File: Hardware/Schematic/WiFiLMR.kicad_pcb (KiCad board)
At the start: 2 copper layers, 50 parts, among them J1 Conn_01x12, J10 Conn_01x02, J2 Conn_01x12, J3 JTAG, J4 Conn_02x04_Odd_Even, J5 Conn_02x02_Odd_Even, J6 Conn_01x12, J7 Conn_01x12, J8 Conn_01x24, J9 Conn_01x02, Q1 Q_PJFET_GSD, U1 TCA8418RTWR, U2 L7805

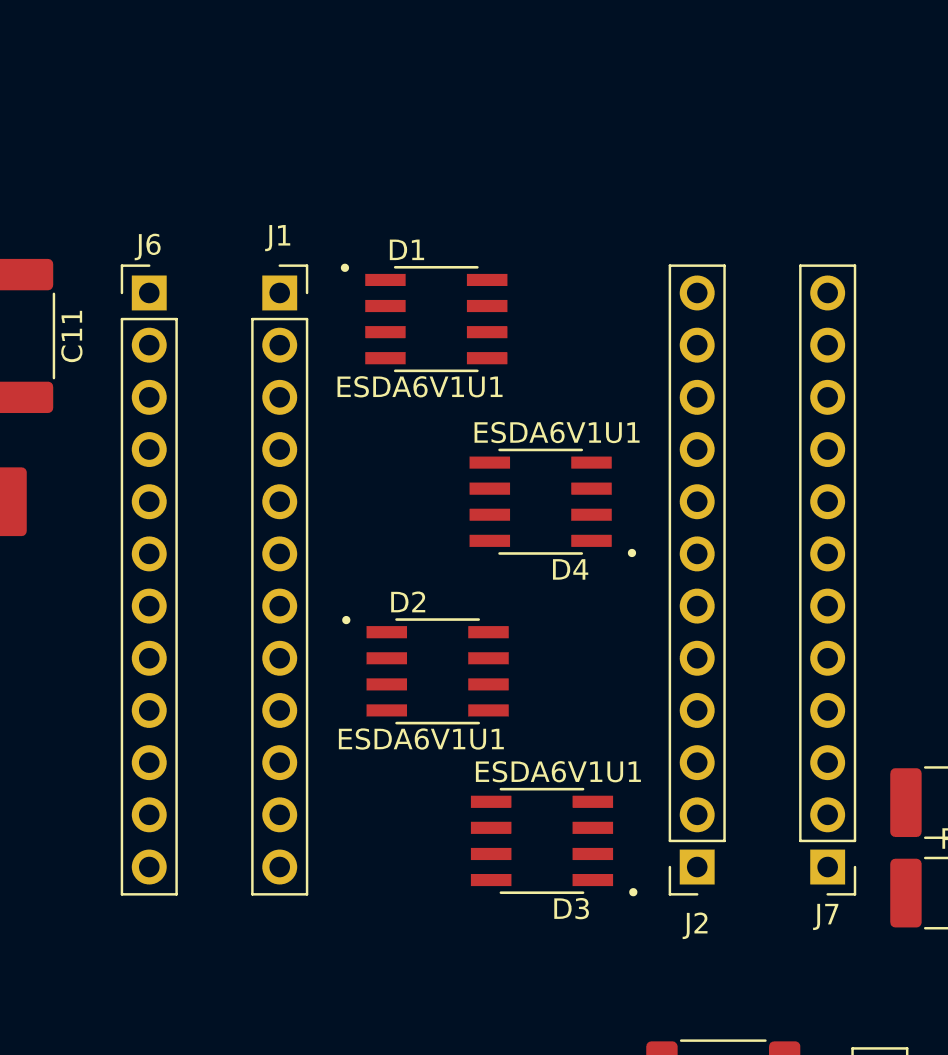
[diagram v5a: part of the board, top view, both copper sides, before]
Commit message: Added pogo-pin test points for "Extra" photon lines. Also added a 32-pin vertical header for connecting multiple smaller boards.
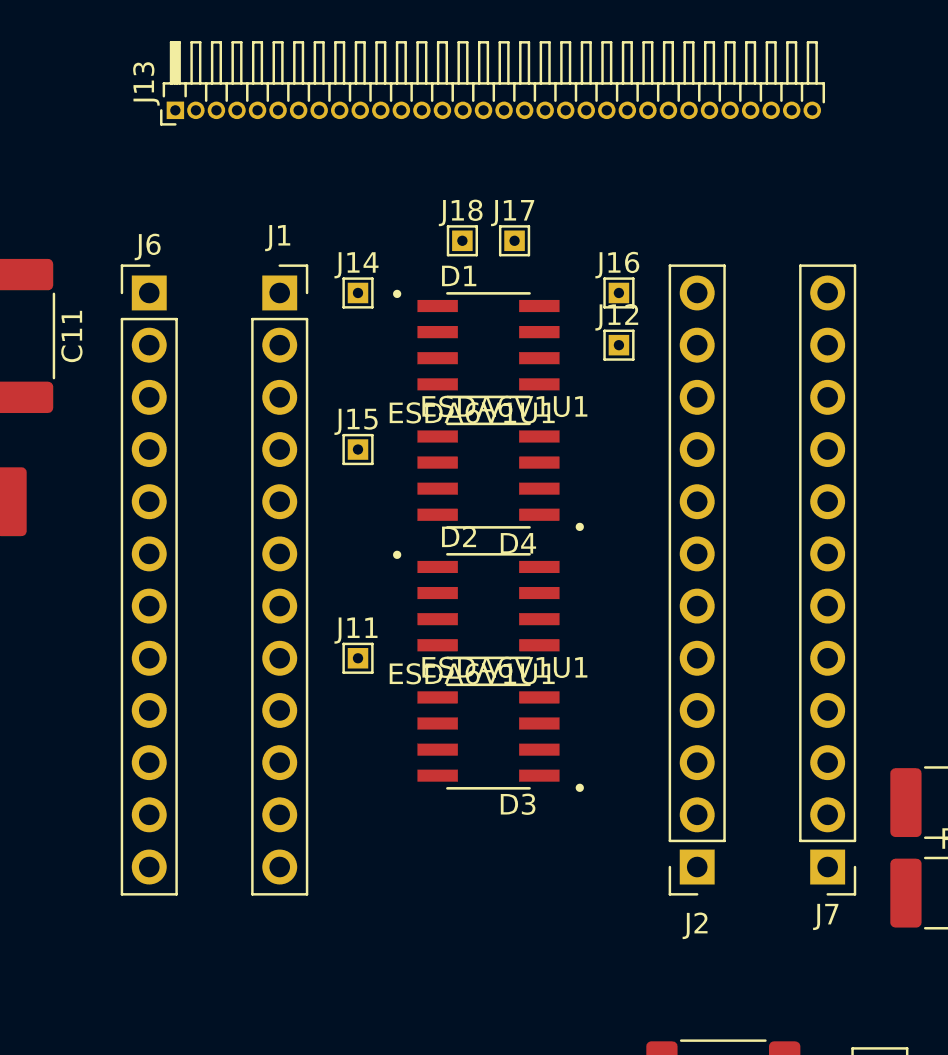
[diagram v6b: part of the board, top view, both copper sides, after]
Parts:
- added J11: Conn_01x01, TestPoint:TestPoint_THTPad_1.0x1.0mm_Drill0.5mm, F.Cu at (132.1, 95.2)
- added J12: Conn_01x01, TestPoint:TestPoint_THTPad_1.0x1.0mm_Drill0.5mm, F.Cu at (144.8, 80.0)
- added J13: Conn_01x32, Connector_PinHeader_1.00mm:PinHeader_1x32_P1.00mm_Horizontal, F.Cu at (123.2, 68.6)
- added J14: Conn_01x01, TestPoint:TestPoint_THTPad_1.0x1.0mm_Drill0.5mm, F.Cu at (132.1, 77.5)
- added J15: Conn_01x01, TestPoint:TestPoint_THTPad_1.0x1.0mm_Drill0.5mm, F.Cu at (132.1, 85.1)
- added J16: Conn_01x01, TestPoint:TestPoint_THTPad_1.0x1.0mm_Drill0.5mm, F.Cu at (144.8, 77.5)
- added J17: Conn_01x01, TestPoint:TestPoint_THTPad_1.0x1.0mm_Drill0.5mm, F.Cu at (139.7, 74.9)
- added J18: Conn_01x01, TestPoint:TestPoint_THTPad_1.0x1.0mm_Drill0.5mm, F.Cu at (137.2, 74.9)
- moved D3 5.71 mm to (138.4, 99.1)
- moved D2 4.03 mm to (138.4, 92.7)
- moved D1 2.84 mm to (138.4, 80.0)
- moved D4 2.84 mm to (138.4, 86.4)
